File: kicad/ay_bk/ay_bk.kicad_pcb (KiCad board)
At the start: 2 copper layers, 40.6 x 54.6 mm, 22 parts, among them J1 AudioJack3, J2 Conn_01x19_Male, SW1 SW_Push, U1 74HCT02, U2 74HCT193, U3 YM2149, Y1 12000 KHZ

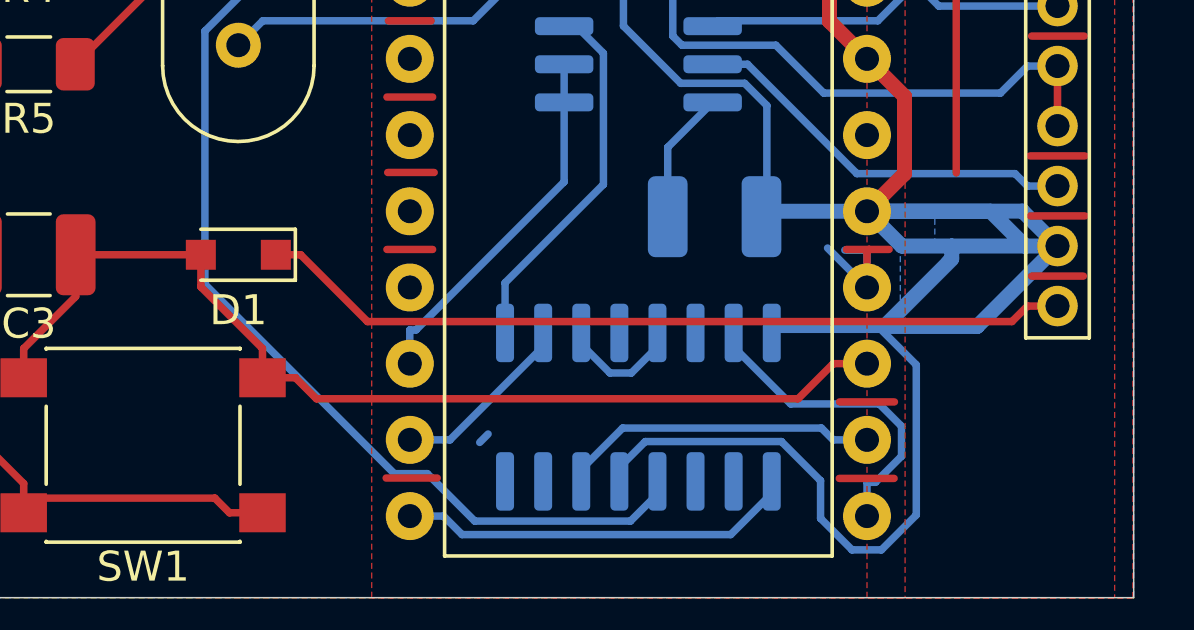
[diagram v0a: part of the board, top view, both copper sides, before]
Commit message: improve reset circuit
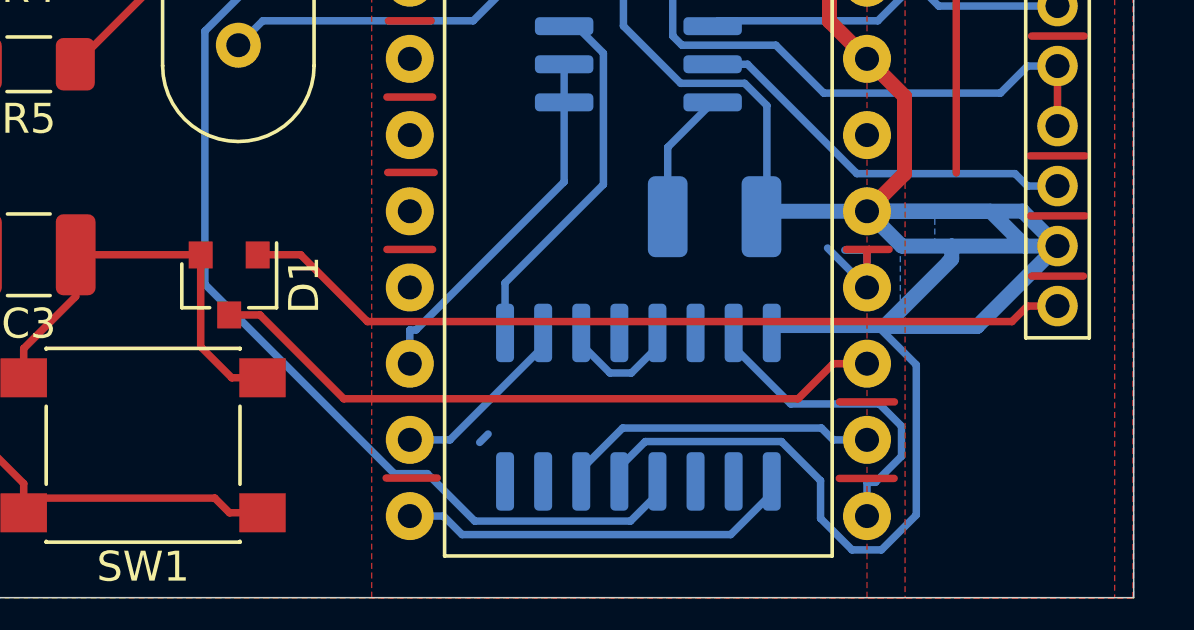
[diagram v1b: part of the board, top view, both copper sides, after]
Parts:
- D1: value BAT54J -> BAT54A; footprint Diode_SMD:D_SOD-323_HandSoldering -> Package_TO_SOT_SMD:SOT-23
- moved D1 1.05 mm to (108.3, 117.2), turned to 270 degrees
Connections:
- U2 pad 12: (no net) -> Net-(U2-Pad12)
- U2 pad 2: (no net) -> Net-(U2-Pad2)
- U2 pad 3: (no net) -> Net-(U2-Pad3)
- U2 pad 7: (no net) -> Net-(U2-Pad7)
- U3 pad 10: (no net) -> Net-(U3-Pad10)
- U3 pad 11: (no net) -> Net-(U3-Pad11)
- U3 pad 12: (no net) -> Net-(U3-Pad12)
- U3 pad 13: (no net) -> Net-(U3-Pad13)
- U3 pad 14: (no net) -> Net-(U3-Pad14)
- U3 pad 15: (no net) -> Net-(U3-Pad15)
- U3 pad 16: (no net) -> Net-(U3-Pad16)
- U3 pad 17: (no net) -> Net-(U3-Pad17)
- U3 pad 2: (no net) -> Net-(U3-Pad2)
- U3 pad 23: Net-(C3-Pad1) -> Net-(D1-Pad3)
- U3 pad 26: (no net) -> Net-(U3-Pad26)
- U3 pad 39: (no net) -> Net-(U3-Pad39)
- U3 pad 5: (no net) -> Net-(U3-Pad5)
- U3 pad 6: (no net) -> Net-(U3-Pad6)
- U3 pad 7: (no net) -> Net-(U3-Pad7)
- U3 pad 8: (no net) -> Net-(U3-Pad8)
- U3 pad 9: (no net) -> Net-(U3-Pad9)
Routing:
- net Net-(D1-Pad3): track 0.00 -> 22.9 mm
- net Net-(C3-Pad1): track 34.9 -> 14.5 mm
- net /RST: track 27.2 -> 27.8 mm
